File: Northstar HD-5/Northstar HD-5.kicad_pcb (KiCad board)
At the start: 2 copper layers, 190.6 x 165 mm, 156 parts, among them J1 MFM data, J2 MFM control, P1 northstar card edge, Q1 2N3904, U1A1 26LS32, U1B1 26LS31, U1C1 74S10, U1D1 74S00, U1E1 50ns_Delay, U1F1 74S04, U1H1 74LS123, U1K1 LM393, U1L1 7438, U1M1 74LS374, U2A1 100ns_Delay, U2B1 74LS161, U2C1 74LS74, U2D1 74LS175, U2E1 82S129, U2F1 74S174, U2H1 74LS283, U2J1 74LS393, U2K1 74LS393, U2L1 2114, U2M1 2114, U3A1 74S74, U3B1 74S02, U3C1 74LS161, U3D1 74LS04, U3E1 74LS161, U3F1 74LS393, U3H1 74LS273, U3J1 74LS193, U3K1 74LS164, U3L1 74LS374, U3M1 74LS166, U4A1 74S74, U4B1 74S02, U4C1 74S74, U4D1 74S04, U4F1 74LS193, U4H1 74LS193, U4J1 74LS04, U4K1 74LS244, U4L1 74LS244, U4M1 74LS244, U5D1 74S124, U5F1 74S74, U5H1 74LS32, U5J1 74LS00, U5K1 74LS279, U5L1 74LS138, U5M1 74LS138

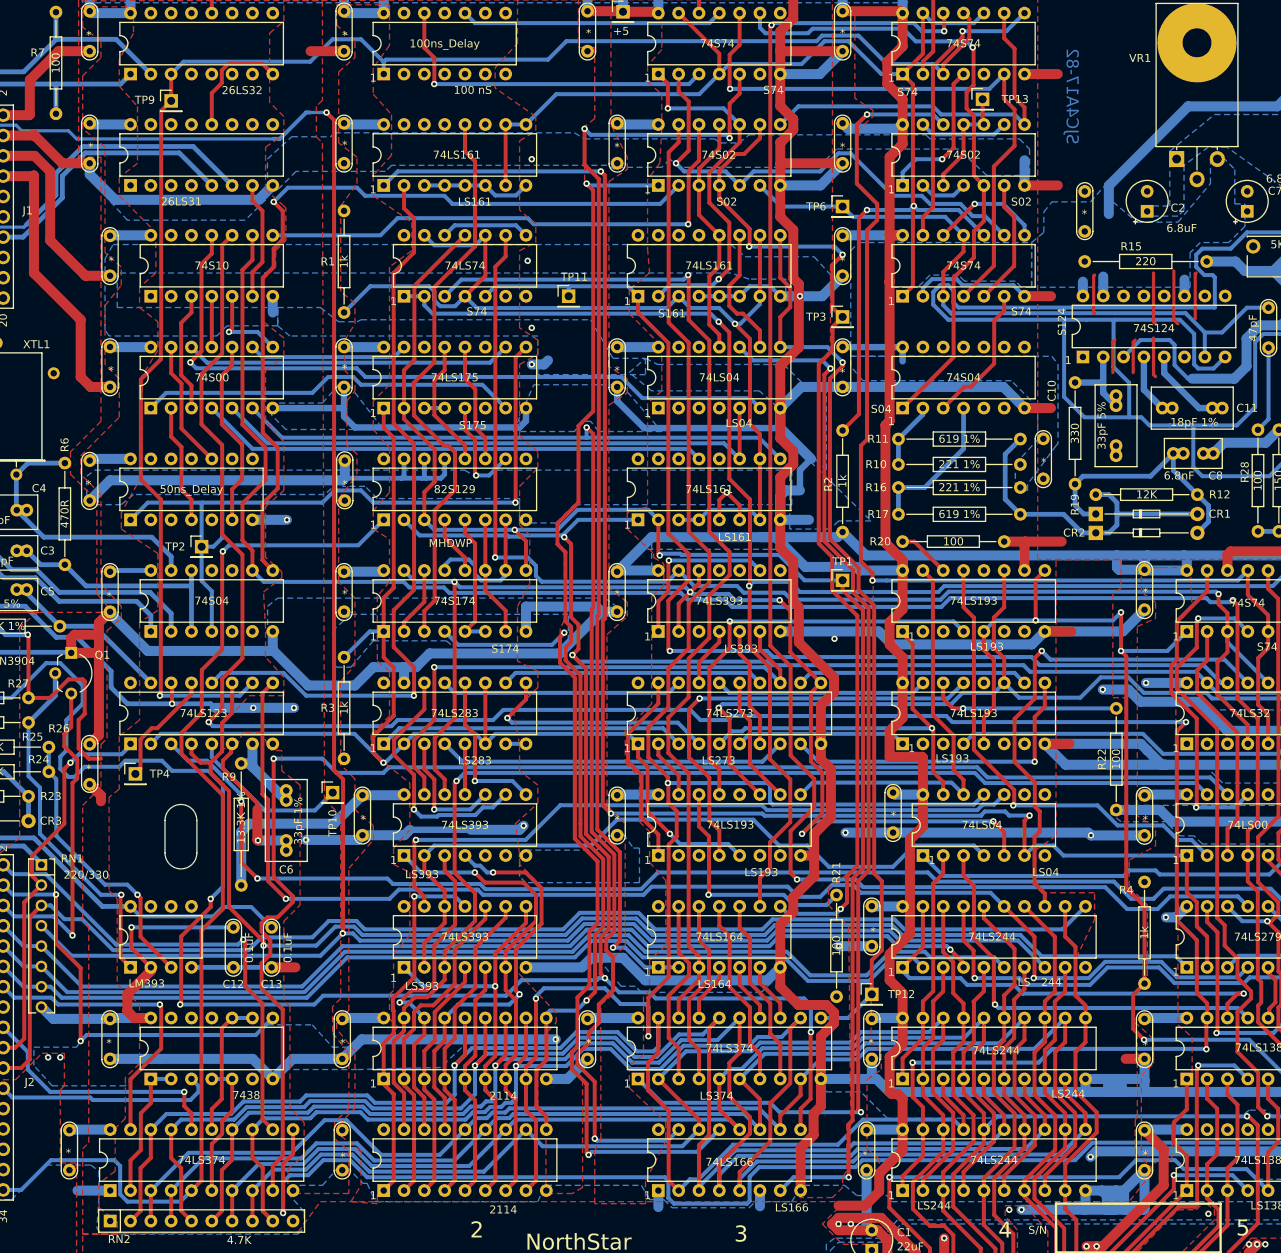
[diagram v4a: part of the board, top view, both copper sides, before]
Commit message: hd5 updates for manugacturing
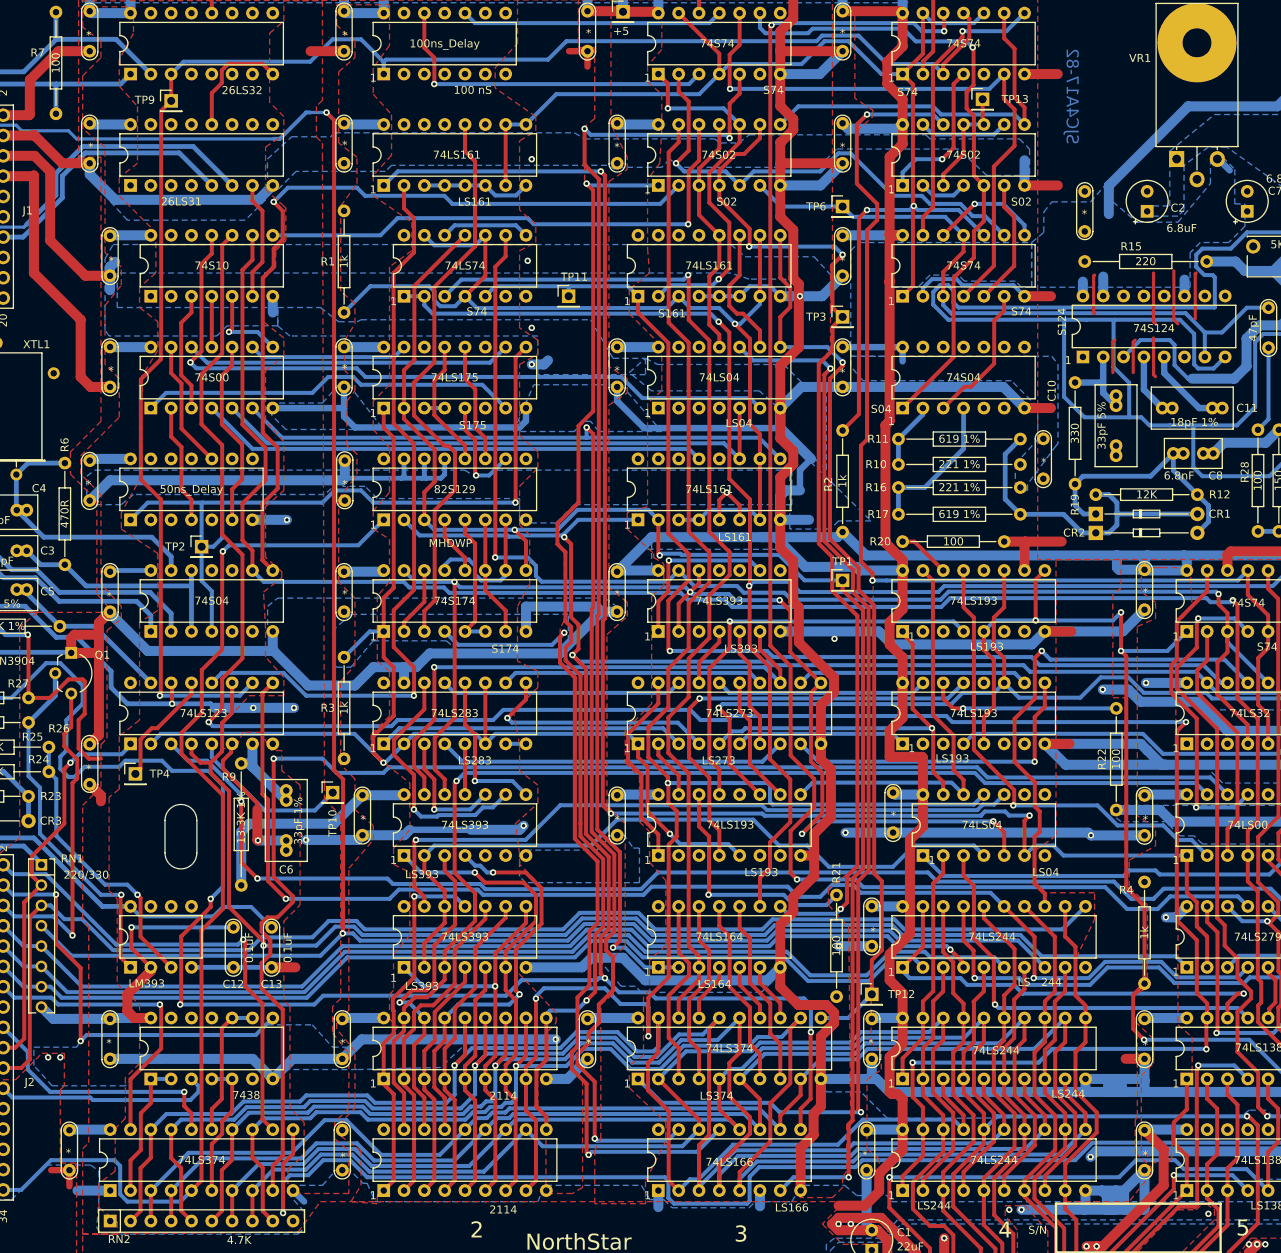
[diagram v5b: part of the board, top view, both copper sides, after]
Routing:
- net GND: track 1858.5 -> 1909.5 mm
- net (no net): track 37.2 -> 0.00 mm
- net +5VP: track 56.8 -> 58.9 mm
- net Net-(TP11-Pad1): track 142.4 -> 140.9 mm
- net /LD CONT: track 194.1 -> 193.3 mm
